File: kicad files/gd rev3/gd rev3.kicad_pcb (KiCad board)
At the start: 4 copper layers, 196 x 192.3 mm, 290 parts, among them J1 XY, J10 Apple_II_Slot, J11 Game Port, J12 Right Angle, J13 SWD, J14 USB_A, J15 Rev2 Header, J16 RP2040 Header, J17 VGA_Micro, J18 vga_SWD, J19 SPKR, J2 DB19_4, J20 Ears, J21 KBD Serial, J22 L77HDE15SD1CH4F, J23 Game-DB VERIFY FOOTPRINT, J3 DB19_16, J4 EN, J5 DSUB19, J6 FDC Hdr, J7 EN, J8 EN, J9 IO-Xtra, Q1 BC817, Q2 BC817, Q3 BC817, Q4 BC817, Q5 BC817, Q6 BC817, Q7 BC817, Q8 BC817, Q9 BC817, SW1 MEGA RESET, SW2 DEV, SW3 IOSEL, SW4 KBD RESET, SW5 KBD Boot Sel, SW6 VGA Boot Sel, SW7 VGA RESET, U1 Apple_MEGA_II, U10 DRAM64KX4, U11 IWM, U12 Slotmaker, U13 74HCT245, U14 RP2040, U15 MIC5504-3.3YM5, U16 74HC245, U17 W25Q128JVS, U18 HCT251, U19 W25Q128JVS, U2 w65c02s, U20 NE556, U21 NE556, U22 74HCT245, U23 RP2040, U24 74LVC2G04, U25 74LVC2G04, U26 MCP4541T, U27 LM4875, U28 SN74LVC573ANS, U29 74LVC2G04, U3 74LVC1G02, U30 74LVC2G04, U31 74LVC2G04-DNP, U32 LM7905_TO220, U35 74LVC2G04, U4 74HCT245, U5 74HCT245, U6 AT28C256-PLCC, U7 DRAM64KX4, U8 DRAM64KX4, U9 DRAM64KX4, X1 14.31818MHz, Y1 ECS-120-18-33-JEM-TR, Y2 ECS-120-18-33-JEM-TR

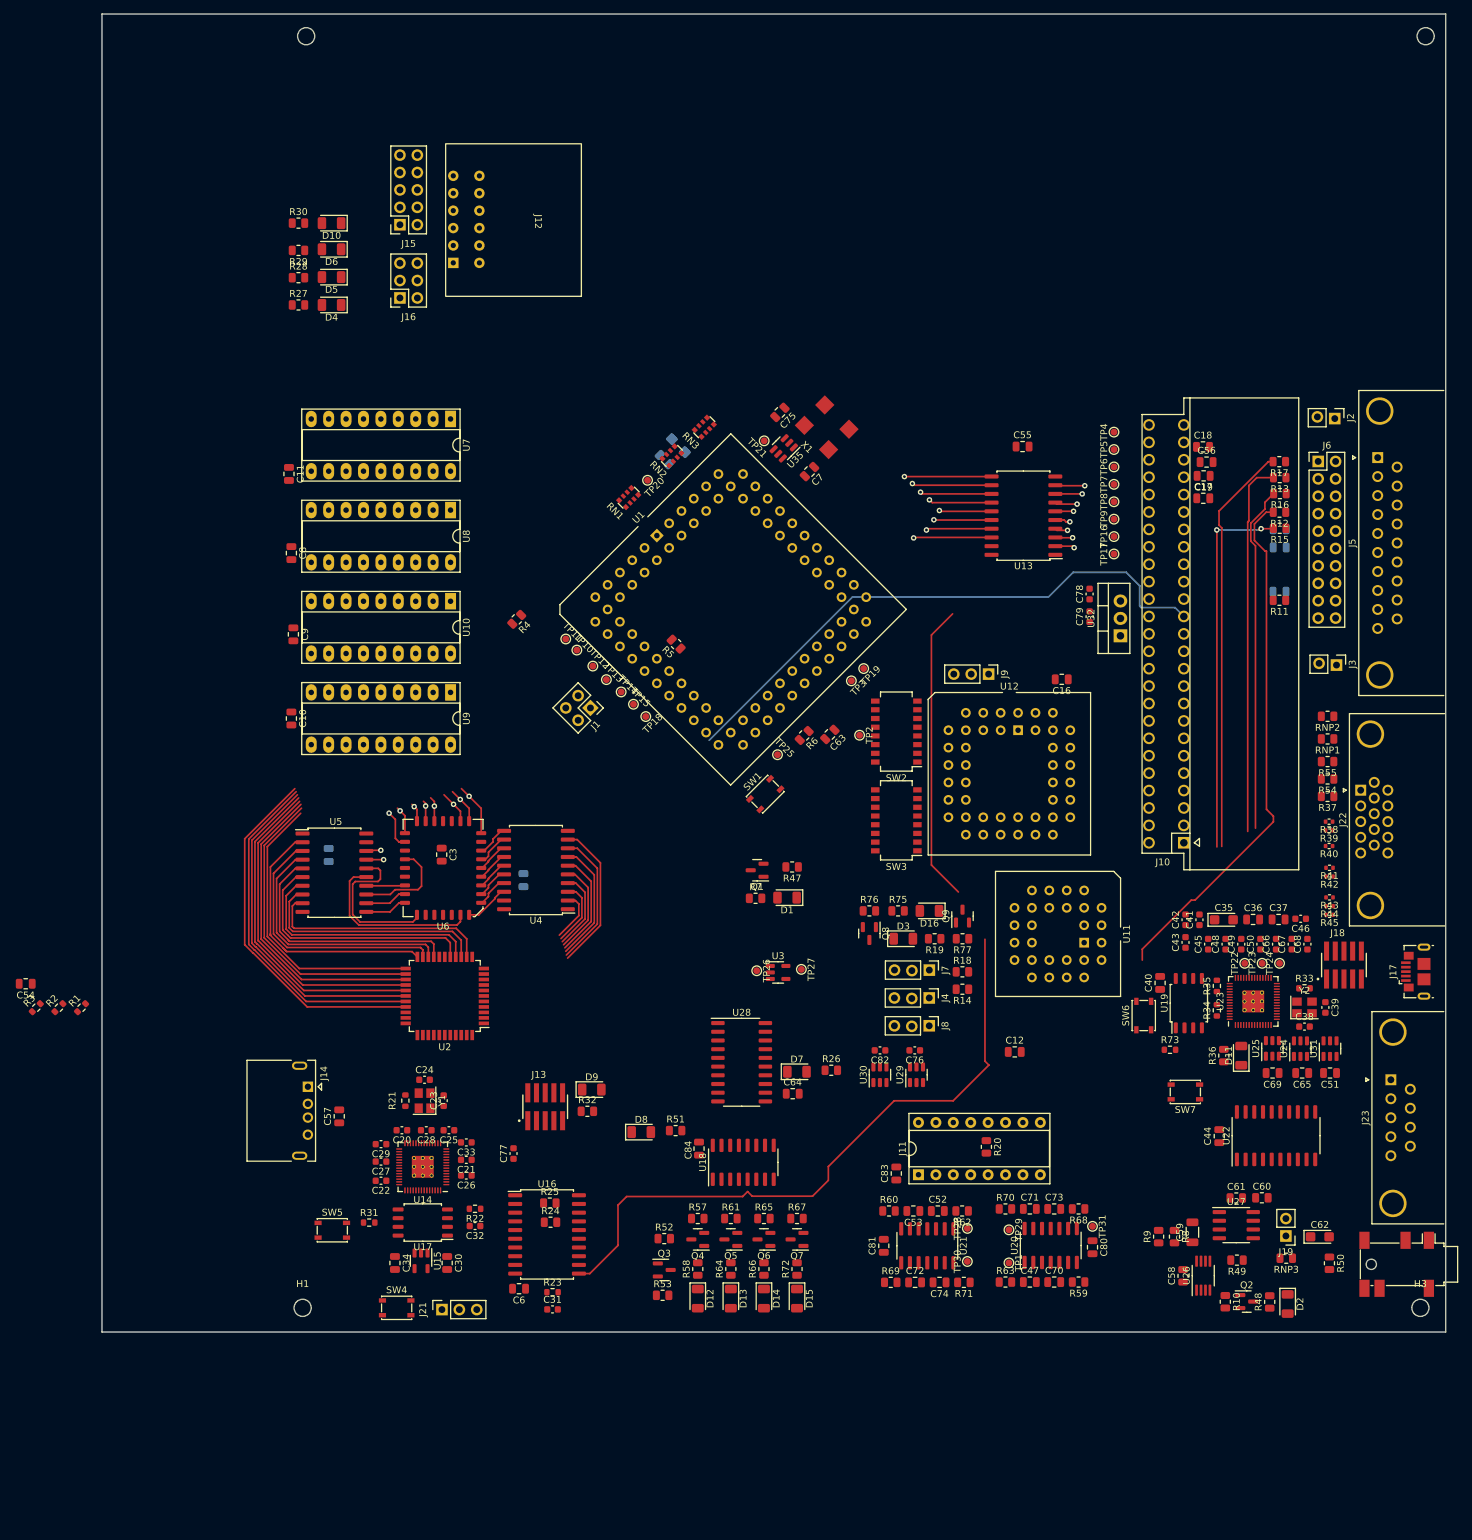
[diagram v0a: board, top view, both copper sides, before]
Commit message: iwm/slot rough routing
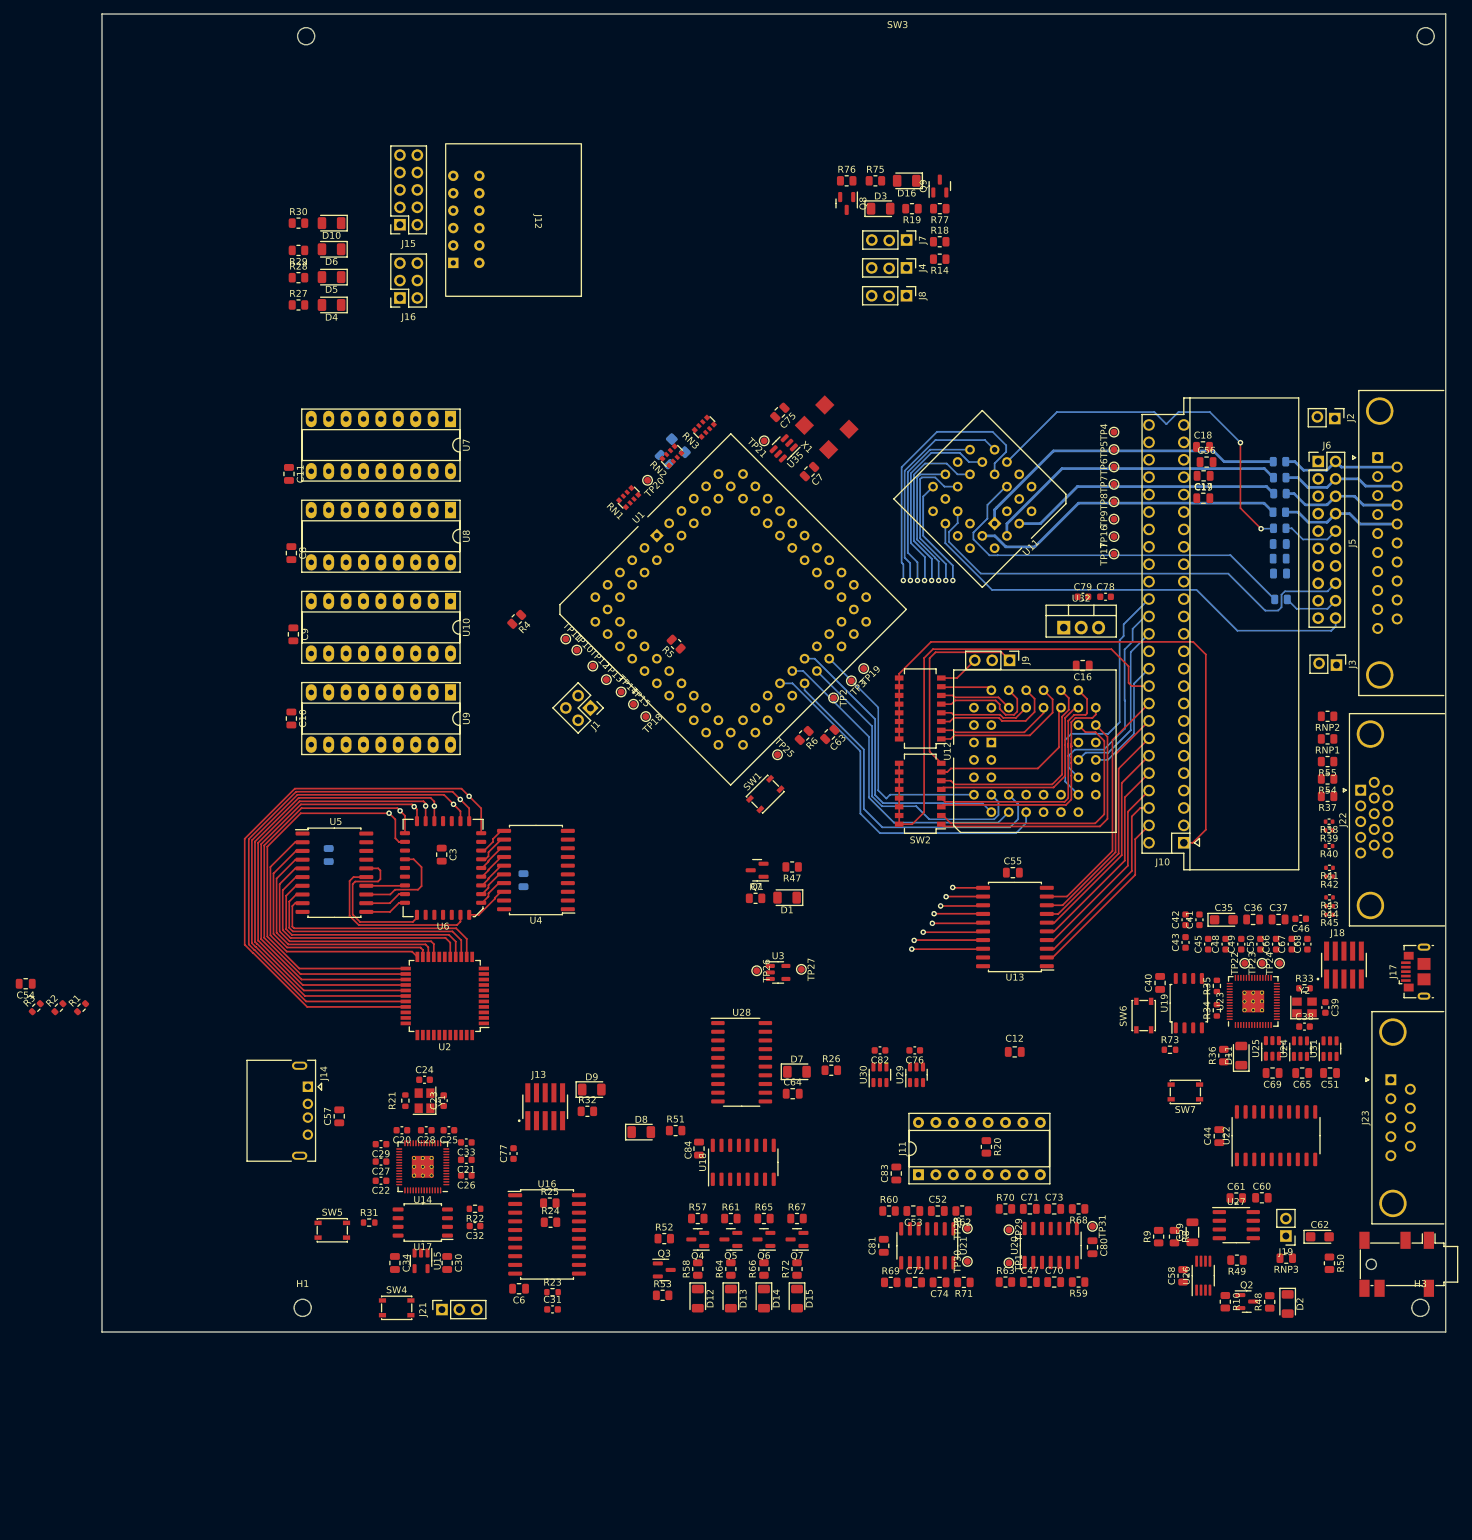
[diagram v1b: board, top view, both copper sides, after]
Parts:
- R11, R12, R13, R15, R16, R17: moved to B.Cu
- moved D3 106.6 mm to (151.4, 54.3)
- moved J7 106.6 mm to (155.2, 58.8)
- moved Q8 106.6 mm to (146.4, 53.5)
- moved R19 106.6 mm to (155.9, 54.3)
- moved R77 106.6 mm to (160.0, 54.3)
- moved J4 106.6 mm to (155.2, 62.9)
- moved J8 106.6 mm to (155.2, 67.0)
- moved R18 106.6 mm to (160.0, 59.1)
- moved D16 106.6 mm to (155.2, 50.2)
- moved Q9 106.6 mm to (160.0, 51.0)
- moved R14 106.6 mm to (160.0, 61.6)
- moved R75 106.6 mm to (150.6, 50.2)
- moved R76 106.6 mm to (146.4, 50.2)
- moved U11 62.5 mm to (168.0, 100.2), turned to -135 degrees
- moved C55 62.2 mm to (170.7, 151.1)
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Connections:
- SW2 pad 1: /Slot/~{DEV7} -> /Slot/~{DEV1}
- SW2 pad 2: /Slot/~{DEV6} -> /Slot/~{DEV2}
- SW2 pad 3: /Slot/~{DEV5} -> /Slot/~{DEV3}
- SW2 pad 5: /Slot/~{DEV3} -> /Slot/~{DEV5}
- SW2 pad 6: /Slot/~{DEV2} -> /Slot/~{DEV6}
- SW2 pad 7: /Slot/~{DEV1} -> /Slot/~{DEV7}
- SW3 pad 1: /Slot/~{IOSEL7} -> /Slot/~{IOSEL1}
- SW3 pad 2: /Slot/~{IOSEL6} -> /Slot/~{IOSEL2}
- SW3 pad 3: /Slot/~{IOSEL5} -> /Slot/~{IOSEL3}
- SW3 pad 5: /Slot/~{IOSEL3} -> /Slot/~{IOSEL5}
- SW3 pad 6: /Slot/~{IOSEL2} -> /Slot/~{IOSEL6}
- SW3 pad 7: /Slot/~{IOSEL1} -> /Slot/~{IOSEL7}
- U2 pad 2: /mega-6502/SYNC_6502 -> /Slot/SYNC_6502
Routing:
- net /IWM/MD3: track 208.0 -> 341.8 mm, vias 2 -> 3
- net /IWM/MD4: track 211.9 -> 333.5 mm, vias 2 -> 3
- net /IWM/MD5: track 210.6 -> 323.9 mm, vias 2 -> 3
- net /IWM/MD6: track 225.7 -> 329.3 mm, vias 2 -> 3
- net /IWM/MD0: track 257.9 -> 360.8 mm, vias 2 -> 3
- net /IWM/MD1: track 254.7 -> 353.1 mm, vias 2 -> 3
- net /IWM/MD2: track 265.3 -> 353.7 mm, vias 2 -> 3
- net /Slot/~{IOSEL}: track 0.00 -> 86.5 mm
- net /IWM/BA12: track 109.5 -> 25.7 mm
- net /Slot/~{DEV}: track 0.00 -> 72.7 mm
- net /IWM/RDATA: track 0.00 -> 68.3 mm
- net /IWM/SENSE: track 0.00 -> 66.6 mm
- net /IWM/WDATA: track 0.00 -> 57.4 mm
- net /Slot/S0: track 0.00 -> 52.5 mm
- net /IWM/MD7: track 365.5 -> 314.8 mm, vias 2 -> 3
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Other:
- board text added: "Move IWM parts (under PS right now) back to near the IWM"
- board text removed: "Swap U11 (IWM) with U13 (Buffer) and move U12 (Slotmaker) down."

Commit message: address bus routed from EPROM to Mega to Slot
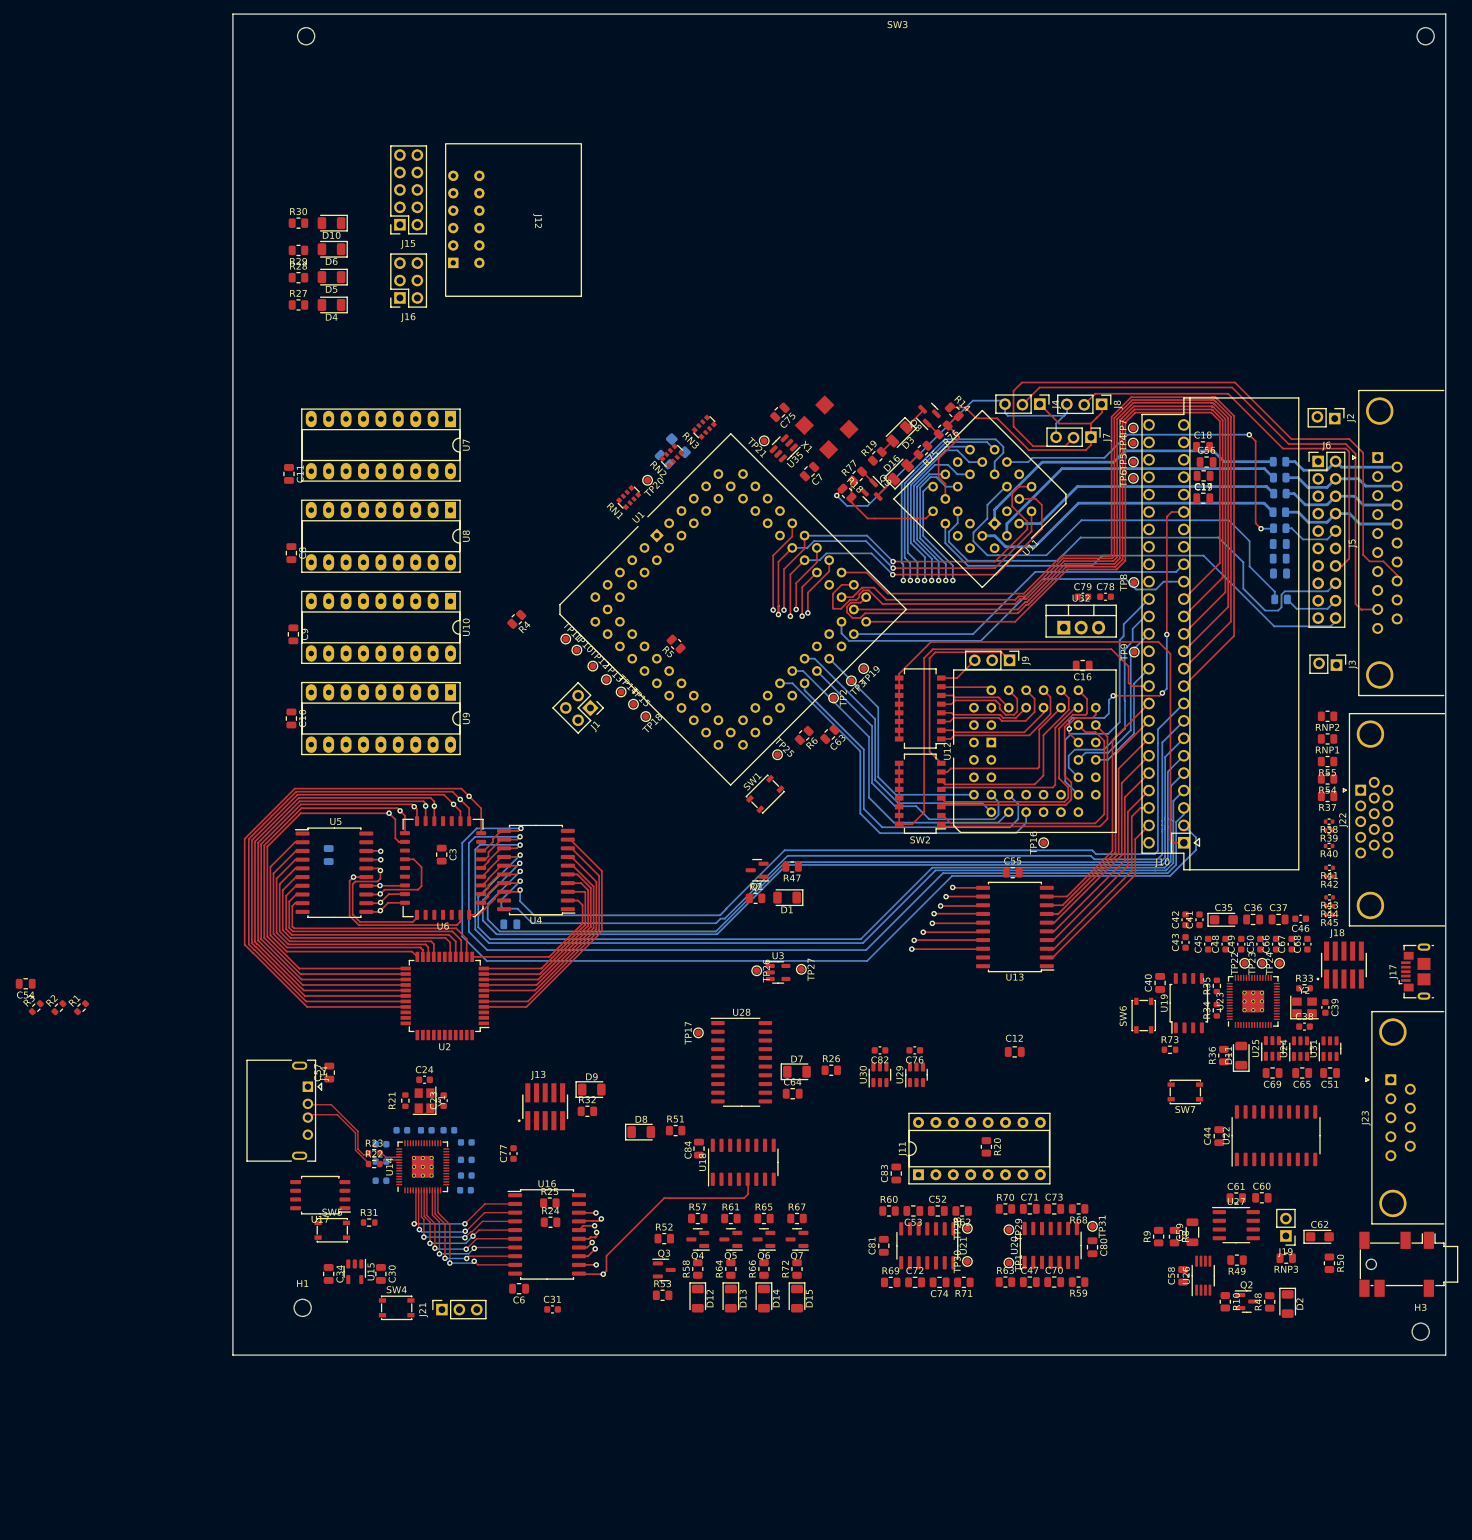
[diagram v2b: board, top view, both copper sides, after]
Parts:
- C20, C21, C22, C25, C26, C27, C28, C29, C32, C33: moved to B.Cu
- moved TP17 92.5 mm to (124.8, 174.5)
- moved TP16 45.8 mm to (175.2, 146.8)
- moved Q9 45.7 mm to (150.4, 95.6), turned to -45 degrees
- moved D16 42.5 mm to (154.3, 92.7), turned to 45 degrees
- moved R77 40.8 mm to (148.0, 93.3), turned to 45 degrees
- moved R75 39.9 mm to (157.5, 89.5), turned to -135 degrees
- moved J7 39.4 mm to (182.1, 87.6)
- moved R18 39.1 mm to (146.5, 95.8), turned to -45 degrees
- moved R76 39.0 mm to (160.5, 86.5), turned to -135 degrees
- moved R19 36.5 mm to (150.9, 90.4), turned to 45 degrees
- moved D3 33.0 mm to (154.1, 87.2), turned to -135 degrees
- moved R23 33.0 mm to (77.5, 192.1)
- moved Q8 32.9 mm to (158.2, 84.2), turned to 135 degrees
- moved J8 32.6 mm to (183.6, 82.8)
- moved J4 27.8 mm to (174.6, 82.8)
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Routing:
- net /IWM/BA2: track 4.01 -> 271.6 mm, vias 0 -> 3
- net /IWM/BA0: track 3.90 -> 269.2 mm, vias 0 -> 2
- net /IWM/BA1: track 4.44 -> 269.3 mm, vias 0 -> 3
- net /IWM/BA3: track 4.02 -> 265.0 mm, vias 0 -> 3
- net /IWM/BA8: track 6.19 -> 251.9 mm, vias 0 -> 1
- net /IWM/BA9: track 6.19 -> 247.7 mm, vias 0 -> 1
- net /IWM/BA10: track 14.2 -> 254.2 mm, vias 0 -> 1
- net /IWM/BA12: track 25.7 -> 259.7 mm, vias 0 -> 1
- net /IWM/BA13: track 22.3 -> 244.4 mm, vias 0 -> 1
- net /IWM/BA11: track 5.58 -> 227.4 mm, vias 0 -> 1
- net /IWM/BA4: track 4.02 -> 220.9 mm, vias 0 -> 2
- net /IWM/BA5: track 3.91 -> 217.8 mm, vias 0 -> 2
- net /IWM/BA6: track 3.88 -> 217.0 mm, vias 0 -> 2
- net /IWM/BA7: track 6.10 -> 212.2 mm, vias 0 -> 1
- net /IWM/BA14: track 0.00 -> 169.2 mm, vias 0 -> 1
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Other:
- board size 196 x 192.3 mm -> 176.9 x 195.7 mm
- board text added: "Do I have Slim 254s still left over?"
- board text removed: "Move 6502 circuit to left and re-route rams."
- board text removed: "Move IWM parts (under PS right now) back to near the IWM"

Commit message: started vga and gameport rough route - may remove vga-usb and move earphone to front
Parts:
- removed C65, C69: 1u, Capacitor_SMD:C_0805_2012Metric
- removed U25: 74LVC2G04, Package_TO_SOT_SMD:SOT-23-6
- removed U31: 74LVC2G04-DNP, Package_TO_SOT_SMD:SOT-23-6
- C35, C36, C37, C41, C42, C43, C45, C46, C48, C49, C50, C66, C67, C68, D11, R36, R73: moved to B.Cu
- moved C12 81.7 mm to (165.9, 95.8)
- moved C76 60.3 mm to (96.2, 181.2)
- moved C82 60.3 mm to (91.1, 181.2)
- moved U29 60.3 mm to (91.1, 184.7)
- moved U30 60.3 mm to (96.4, 184.7)
- moved C54 51.5 mm to (77.6, 174.7)
- moved R1 51.5 mm to (85.8, 178.2)
- moved R2 51.5 mm to (82.5, 178.2)
- moved R3 51.5 mm to (79.2, 178.2)
- moved U22 31.5 mm to (182.7, 172.2), turned to 0 degrees
- moved SW7 24.4 mm to (219.6, 177.5), turned to 0 degrees
- moved TP22 21.0 mm to (225.1, 160.7), turned to -90 degrees
- moved C51 20.9 mm to (196.7, 175.4)
- moved C44 20.5 mm to (182.6, 180.2), turned to 180 degrees
- moved R73 18.6 mm to (197.1, 158.7), turned to 180 degrees
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- renumbered U30 to U29, U29 to U30
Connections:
- U22 pad 18: /video/SERVID_RP -> /video/~{RESET_RP}
- U22 pad 2: /mega-6502/SERVID -> /video/~{RESET}
- U23 pad 14: /video/SERVID_RP -> unconnected-(U23-Pad14)
- U23 pad 15: /video/7M_RP -> unconnected-(U23-Pad15)
- U29 pad 3: /IWM/~{RESET} -> /rp2040-keyboard/~{PH0}
- U29 pad 4: Net-(U29-Pad1) -> /rp2040-keyboard/PH0rp
- U30 pad 1: Net-(U29-Pad1) -> Net-(U30-Pad1)
- U30 pad 3: /rp2040-keyboard/~{PH0} -> /IWM/~{RESET}
- U30 pad 4: /rp2040-keyboard/PH0rp -> Net-(U30-Pad1)
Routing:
- net /game_port/SW1_CAPL: track 0.00 -> 93.5 mm
- net /mega-6502/RGB4: track 0.00 -> 87.4 mm
- net /mega-6502/RGB1: track 0.00 -> 86.1 mm
- net /game_port/SW0_OAPL: track 0.00 -> 84.3 mm
- net /game_port/SW2: track 0.00 -> 83.2 mm
- net /mega-6502/RGB8: track 0.00 -> 77.6 mm
- net /mega-6502/RGB2: track 0.00 -> 72.6 mm
- net /game_port/PDL3: track 0.00 -> 66.4 mm
- net /game_port/PDL0: track 0.00 -> 64.9 mm
- net /game_port/PDL1: track 0.00 -> 60.3 mm
- net /game_port/PDL2: track 0.00 -> 56.0 mm
- net /Slot/AN0: track 0.00 -> 55.4 mm
- net /Slot/AN2: track 0.00 -> 54.1 mm
- net /Slot/AN1: track 0.00 -> 51.8 mm
- net /Slot/AN3: track 0.00 -> 50.7 mm
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
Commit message: need to move vga to prevent long 14M route
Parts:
- moved C2 10.4 mm to (81.2, 148.5)
- moved U5 10.4 mm to (82.0, 151.1)
- moved C1 10.4 mm to (107.7, 158.6)
- moved C3 10.4 mm to (97.7, 148.5)
- moved U2 10.4 mm to (98.1, 169.1)
- moved U4 10.4 mm to (111.4, 150.7)
- moved U6 10.4 mm to (97.9, 150.4)
- moved C10 8.70 mm to (74.1, 128.5)
- moved C8 8.70 mm to (74.1, 104.4)
- moved U10 8.70 mm to (97.3, 111.4)
- moved U7 8.70 mm to (97.3, 84.8)
- moved U8 8.70 mm to (97.3, 98.1)
- moved U9 8.70 mm to (97.3, 124.7)
- moved C11 8.70 mm to (73.8, 92.8)
- moved C9 8.70 mm to (74.4, 116.2)
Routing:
- net /IWM/BA7: track 212.2 -> 191.5 mm
- net /IWM/BA1: track 269.3 -> 248.5 mm
- net /IWM/BA0: track 269.2 -> 248.6 mm
- net /IWM/BA5: track 217.8 -> 197.9 mm
- net /IWM/BA6: track 217.0 -> 197.2 mm
- net /IWM/BA3: track 265.0 -> 245.4 mm
- net /IWM/BA2: track 271.6 -> 252.5 mm
- net /IWM/BA4: track 220.9 -> 202.4 mm
- net /IWM/MD7: track 433.7 -> 420.4 mm
- net /IWM/MD6: track 409.3 -> 396.3 mm
- net /IWM/MD2: track 404.0 -> 393.2 mm
- net /mega-6502/14M: track 0.00 -> 10.7 mm
- net /IWM/BA9: track 247.7 -> 237.7 mm
- net /IWM/BA13: track 244.4 -> 234.4 mm
- net /IWM/BA10: track 254.2 -> 244.2 mm
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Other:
- board outline removed
